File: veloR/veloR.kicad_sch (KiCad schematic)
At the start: 42 parts, among them J3 DISPLAY, J4 Conn_01x10, J9 Programador, M1 M1, M2 M2, SW1 SW_DPST_x2, SW10 SW_Push, U3 AMS1117-3.3, U6 ESP32-WROOM-32, U7 AMS1117-5.0

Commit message: Add files via upload
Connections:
- net M3: now reaches C16.1, DrivTA6586-1.7 (S1), DrivTA6586-1.8 (S1), M1.2 (Pin_2)
- net M4: now reaches C16.2, DrivTA6586-1.5 (S2), DrivTA6586-1.6 (S2), M1.1 (Pin_1)
- net M2: now reaches C15.2, DrivTA6586-2.5 (S2), DrivTA6586-2.6 (S2), M2.1 (Pin_1)
- net M1: now reaches C15.1, DrivTA6586-2.7 (S1), DrivTA6586-2.8 (S1), M2.2 (Pin_2)
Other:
- note added: "ALIMENTACION"
- note added: "BOTONES"
- note added: "DRIVERS"
- note added: "EN Y BOOT"
- note added: "INTERRUPTOR"
- note added: "LED INDICATIVO"
- note added: "QTR8A"
- moved on the sheet: Alimentacion1, C1, C13, C14, C15, C16, C2, C6, DrivTA6586-1, DrivTA6586-2, H1, H2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

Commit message: Add files via upload
MODIFIQUE PANTALLA,  ACOMODE COSAS, ETC
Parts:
- added D1: D, Diode_SMD:D_SMA, symbol Device:D
- added R5, R8: 10k, Resistor_SMD:R_1206_3216Metric_Pad1.30x1.75mm_HandSolder, symbol EESTN5:R
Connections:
- net +5V: now also D1.1 (K); no longer J4.1 (Pin_1), J9.3
- net 3V3: now also J4.1 (Pin_1), R5.1, R8.1
- net INA2: now also U6.27 (IO17); no longer U6.34 (IO5)
- net SCL: now also R8.2
- net SDA: now also R5.2
- new net: D1.2 (A), J9.3
- no-connect marks 1 -> 2
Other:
- moved on the sheet: Alimentacion1, C1, C10, C11, C12, C13, C14, C15, C16, C2, C3, C4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

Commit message: Add files via upload
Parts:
- added M3, M4: Motor_DC, NUEVAS HUELLAS TREJO:motor 3600rpm, symbol Motor:Motor_DC
- C1, C13: footprint Capacitor_SMD:C_Elec_4x5.4 -> Capacitor_SMD:C_Elec_10x10.2
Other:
- moved on the sheet: Alimentacion1, C1, C10, C11, C12, C13, C14, C15, C16, C2, C3, C4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

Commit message: Add files via upload
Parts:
- J4: footprint Connector_PinHeader_2.54mm:PinHeader_1x10_P2.54mm_Horizontal -> Connector_JST:JST_XH_S10B-XH-A-1_1x10_P2.50mm_Horizontal
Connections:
- net 3V3: now also J4.10 (Pin_10); no longer J4.1 (Pin_1)
- net D1: now also J4.2 (Pin_2); no longer J4.9 (Pin_9)
- net D2: now also J4.3 (Pin_3); no longer J4.8 (Pin_8)
- net D3: now also J4.4 (Pin_4); no longer J4.7 (Pin_7)
- net D4: now also J4.5 (Pin_5); no longer J4.6 (Pin_6)
- net D5: now also J4.6 (Pin_6); no longer J4.5 (Pin_5)
- net D6: now also J4.7 (Pin_7); no longer J4.4 (Pin_4)
- net D7: now also J4.8 (Pin_8); no longer J4.3 (Pin_3)
- net D8: now also J4.9 (Pin_9); no longer J4.2 (Pin_2)
- net GND: now also J4.1 (Pin_1); no longer J4.10 (Pin_10)
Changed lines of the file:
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@@
 		(polyline
 			(pts
-				(xy 205.74 112.395) (xy 175.26 112.395) (xy 175.26 135.255) (xy 205.74 135.255)
+				(xy 174.625 149.225) (xy 174.625 159.385) (xy 206.375 159.385) (xy 206.375 149.225)
 			)
 			(stroke
@@
 		(polyline
 			(pts
-				(xy 102.87 43.815) (xy 80.645 43.815) (xy 80.645 66.675) (xy 102.87 66.675)
+				(xy 212.09 93.345) (xy 212.09 135.255) (xy 265.43 135.255) (xy 265.43 93.345)
 			)
 			(stroke
@@
 		(polyline
 			(pts
-				(xy 212.09 93.345) (xy 212.09 135.255) (xy 265.43 135.255) (xy 265.43 93.345)
+				(xy 205.74 112.395) (xy 175.26 112.395) (xy 175.26 135.255) (xy 205.74 135.255)
 			)
 			(stroke
@@
 		(polyline
 			(pts
-				(xy 50.165 156.845) (xy 99.695 156.845) (xy 99.695 111.125) (xy 50.165 111.125)
+				(xy 132.08 112.395) (xy 132.08 135.255) (xy 170.18 135.255) (xy 170.18 112.395)
 			)
 			(stroke
@@
 		(polyline
 			(pts
-				(xy 60.96 70.485) (xy 60.96 108.585) (xy 104.14 108.585) (xy 104.14 70.485)
+				(xy 50.165 156.845) (xy 99.695 156.845) (xy 99.695 111.125) (xy 50.165 111.125)
 			)
 			(stroke
@@
 		(polyline
 			(pts
-				(xy 174.625 149.225) (xy 174.625 159.385) (xy 206.375 159.385) (xy 206.375 149.225)
+				(xy 132.08 136.525) (xy 132.08 159.385) (xy 170.18 159.385) (xy 170.18 136.525)
 			)
 			(stroke
@@
 		(polyline
 			(pts
-				(xy 132.08 136.525) (xy 132.08 159.385) (xy 170.18 159.385) (xy 170.18 136.525)
+				(xy 174.625 136.525) (xy 174.625 147.955) (xy 206.375 147.955) (xy 206.375 136.525)
 			)
 			(stroke
@@
 		(polyline
 			(pts
-				(xy 106.045 38.735) (xy 106.045 108.585) (xy 173.355 108.585) (xy 173.355 38.735)
+				(xy 127 116.84) (xy 102.87 116.84) (xy 102.87 144.78) (xy 127 144.78)
 			)
 			(stroke
@@
 		(polyline
 			(pts
-				(xy 212.09 158.115) (xy 248.92 158.115) (xy 248.92 137.795) (xy 212.09 137.795)
+				(xy 106.045 38.735) (xy 106.045 108.585) (xy 173.355 108.585) (xy 173.355 38.735)
 			)
 			(stroke
@@
 		(polyline
 			(pts
-				(xy 127 116.84) (xy 102.87 116.84) (xy 102.87 144.78) (xy 127 144.78)
+				(xy 212.09 158.115) (xy 248.92 158.115) (xy 248.92 137.795) (xy 212.09 137.795)
 			)
 			(stroke
@@
 		(polyline
 			(pts
-				(xy 174.625 136.525) (xy 174.625 147.955) (xy 206.375 147.955) (xy 206.375 136.525)
+				(xy 102.87 43.815) (xy 80.645 43.815) (xy 80.645 66.675) (xy 102.87 66.675)
 			)
 			(stroke
@@
 		(polyline
 			(pts
-				(xy 132.08 112.395) (xy 132.08 135.255) (xy 170.18 135.255) (xy 170.18 112.395)
+				(xy 60.96 70.485) (xy 60.96 108.585) (xy 104.14 108.585) (xy 104.14 70.485)
 			)
 			(stroke
@@
 	(symbol
 		(lib_id "Connector_Generic:Conn_01x10")
-		(at 229.87 146.05 90)
+		(at 232.41 146.05 270)
+		(mirror x)
 		(unit 1)
 		(exclude_from_sim no)
@@
 		(on_board yes)
 		(dnp no)
-		(fields_autoplaced yes)
 		(property "Reference" "J4"
 			(at 231.14 139.7 90)
@@
 			)
 		)
-		(property "Footprint" "Connector_PinHeader_2.54mm:PinHeader_1x10_P2.54mm_Horizontal"
-			(at 229.87 146.05 0)
+		(property "Footprint" "Connector_JST:JST_XH_S10B-XH-A-1_1x10_P2.50mm_Horizontal"
+			(at 232.41 146.05 0)
 			(effects
 				(font
@@
 		)
 		(property "Datasheet" "~"
-			(at 229.87 146.05 0)
+			(at 232.41 146.05 0)
 			(effects
 				(font
@@
 		)
 		(property "Description" "Generic connector, single row, 01x10, script generated (kicad-library-utils/schlib/autogen/connector/)"
-			(at 229.87 146.05 0)
+			(at 232.41 146.05 0)
 			(effects
 				(font

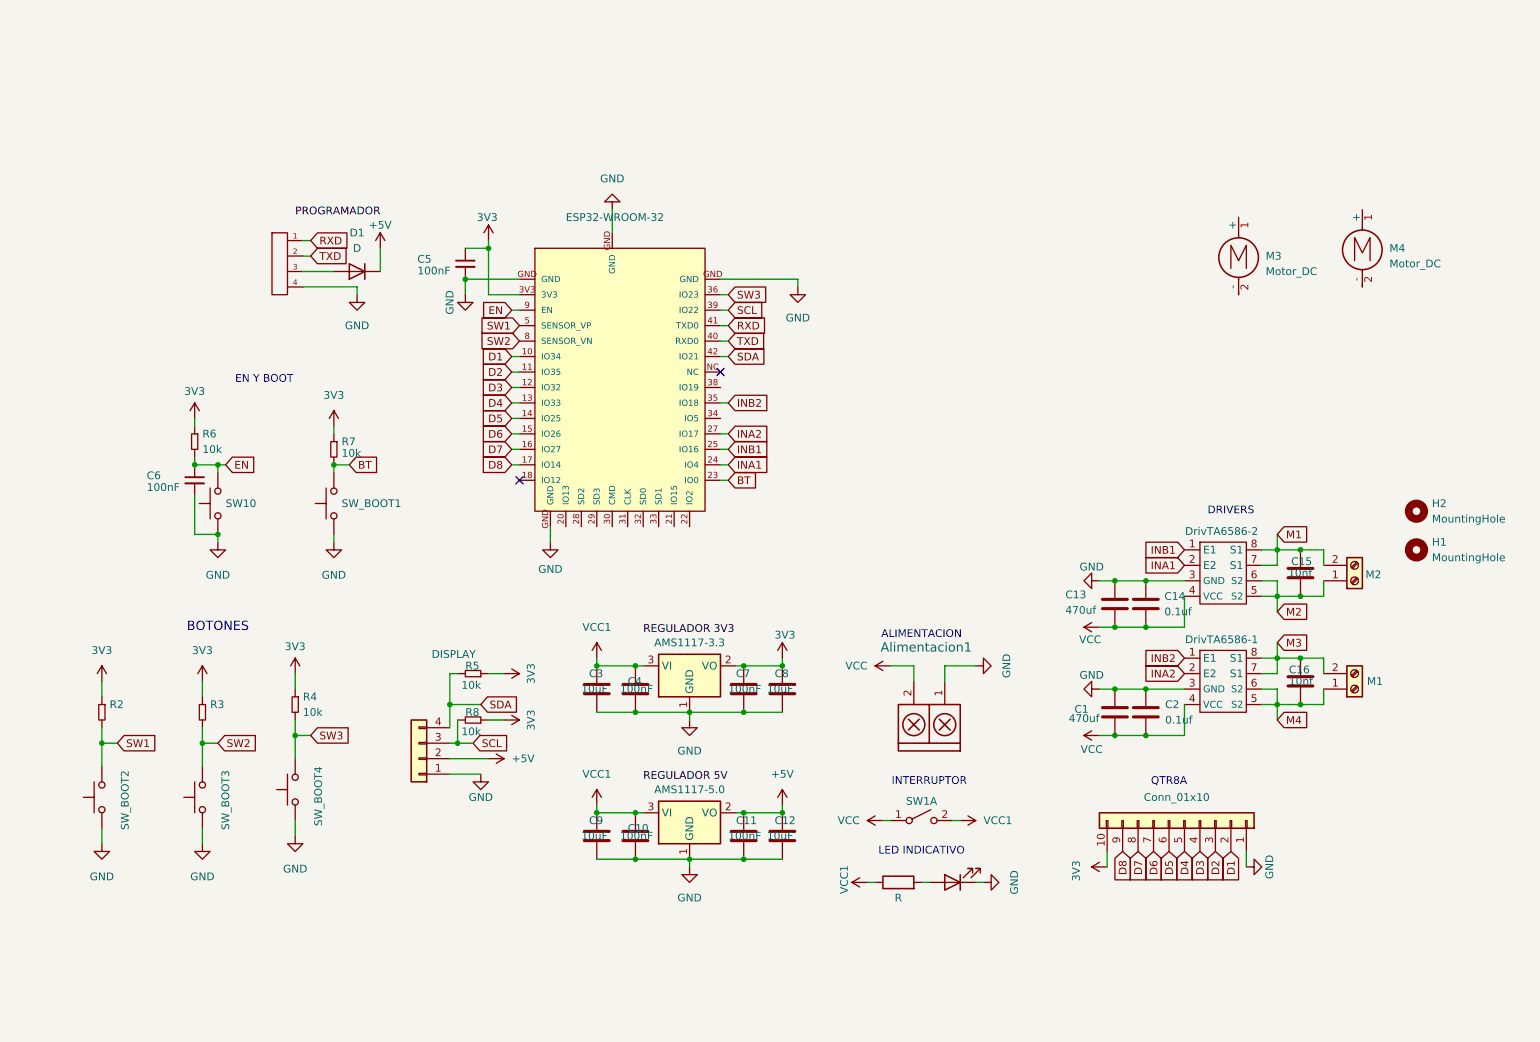
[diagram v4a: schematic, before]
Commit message: Add files via upload
en este archivo se cambio los reguladores de tension por step down mini 360
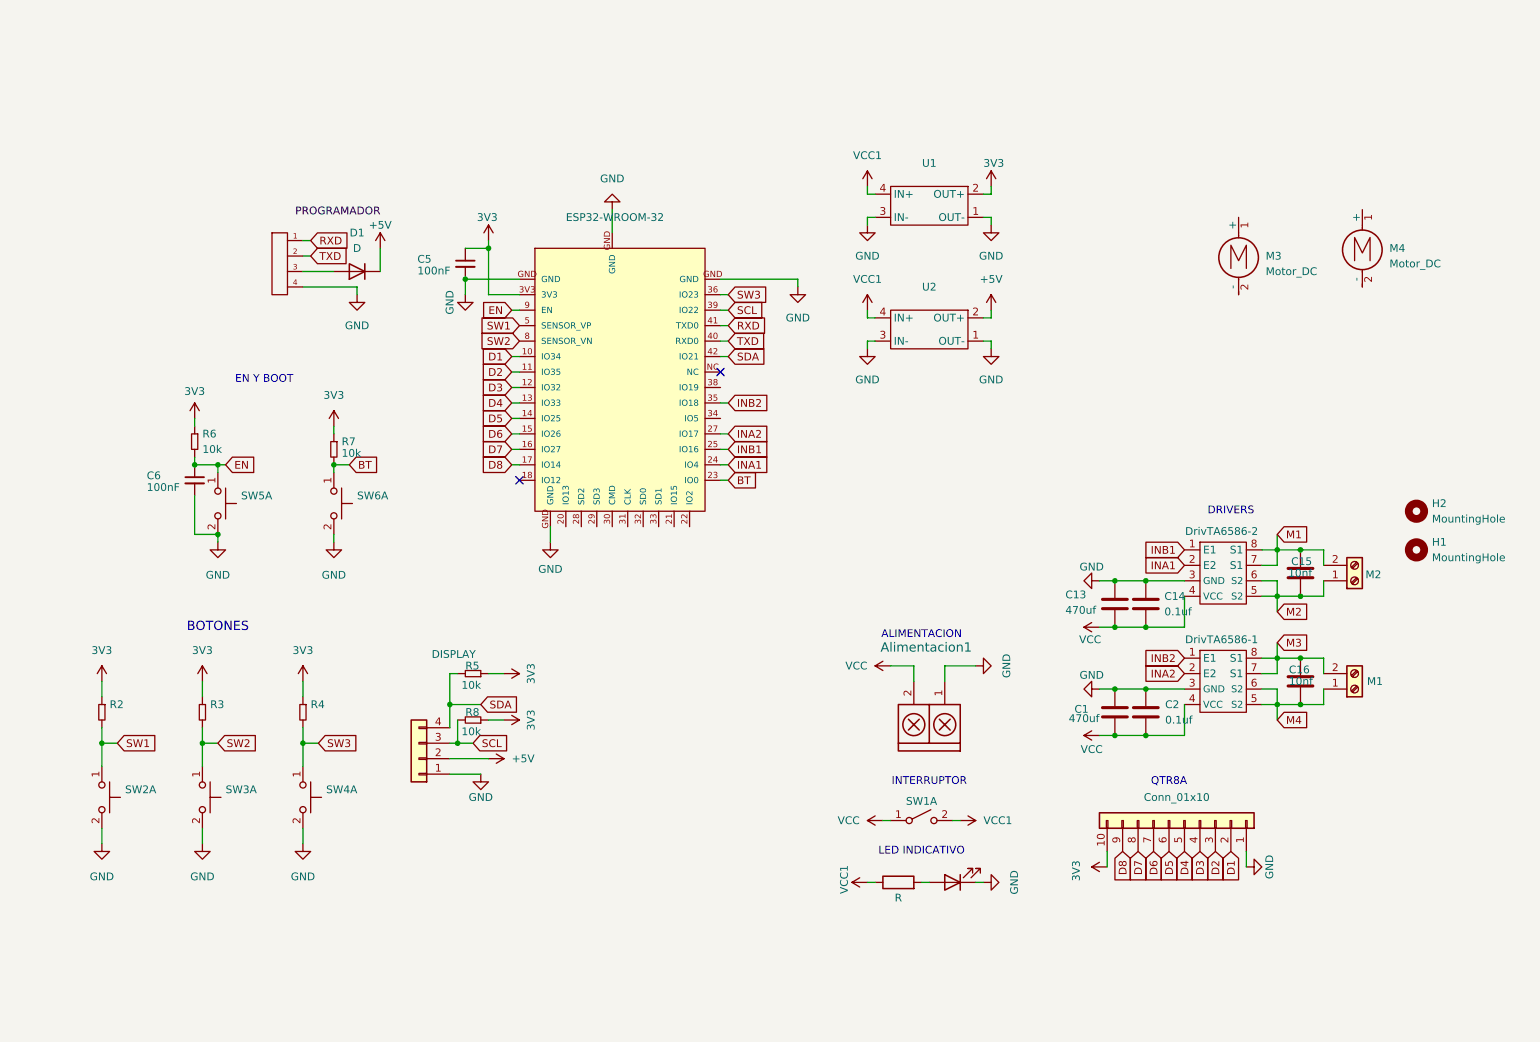
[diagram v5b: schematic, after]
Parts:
- removed C10, C11, C4, C7: 100nF, Capacitor_SMD:C_0805_2012Metric, symbol Device:C
- removed C12, C3, C8, C9: 10uF, Capacitor_SMD:C_0805_2012Metric, symbol Device:C
- removed SW10, SW_BOOT1: SW_Push, EESTN5:Pulsador_SMD_2_ALTO, symbol EESTN5:SW_Push
- removed SW_BOOT2, SW_BOOT3, SW_BOOT4: SW_Push, MacroLib:Button, symbol EESTN5:SW_Push
- removed U3: AMS1117-3.3, Package_TO_SOT_SMD:SOT-223-3_TabPin2, symbol Regulator_Linear:AMS1117-5.0
- removed U7: AMS1117-5.0, Package_TO_SOT_SMD:SOT-223-3_TabPin2, symbol Regulator_Linear:AMS1117-5.0
- added SW2, SW3, SW4, SW5, SW6: SW_Push_Dual_x2, NUEVAS HUELLAS TREJO:SW 6MM 2 PIN, symbol Switch:SW_Push_Dual_x2
- added U1, U2: ~, NUEVAS HUELLAS TREJO:STEP DOWN MINI 360, symbol Trejo huellas nuevas:STEP_DOWN_MINI_360
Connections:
- net +5V: now also U2.2 (OUT+)
- net 3V3: now also U1.2 (OUT+)
- net BT: now also SW6.1 (C)
- net EN: now also SW5.1 (C)
- net GND: now also SW2.2 (D), SW3.2 (D), SW4.2 (D), SW5.2 (D), SW6.2 (D), U1.1 (OUT-), U1.3 (IN-), U2.1 (OUT-), U2.3 (IN-)
- net SW1: now also SW2.1 (C)
- net SW2: now also SW3.1 (C)
- net SW3: now also SW4.1 (C)
- net VCC1: now also U1.4 (IN+), U2.4 (IN+)
